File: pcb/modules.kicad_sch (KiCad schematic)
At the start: 20 parts, among them J2 Conn_01x08_Pin, J3 Conn_Coaxial, J4 Conn_Coaxial, Q2 2N7002, U4 BME280, U6 NEO-M8M, U7 E220-900T22S

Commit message: Finishing schematic and updating PCB
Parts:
- D2: footprint (none) -> LED_SMD:LED_Cree-XP-G
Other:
- moved on the sheet: C18, C19

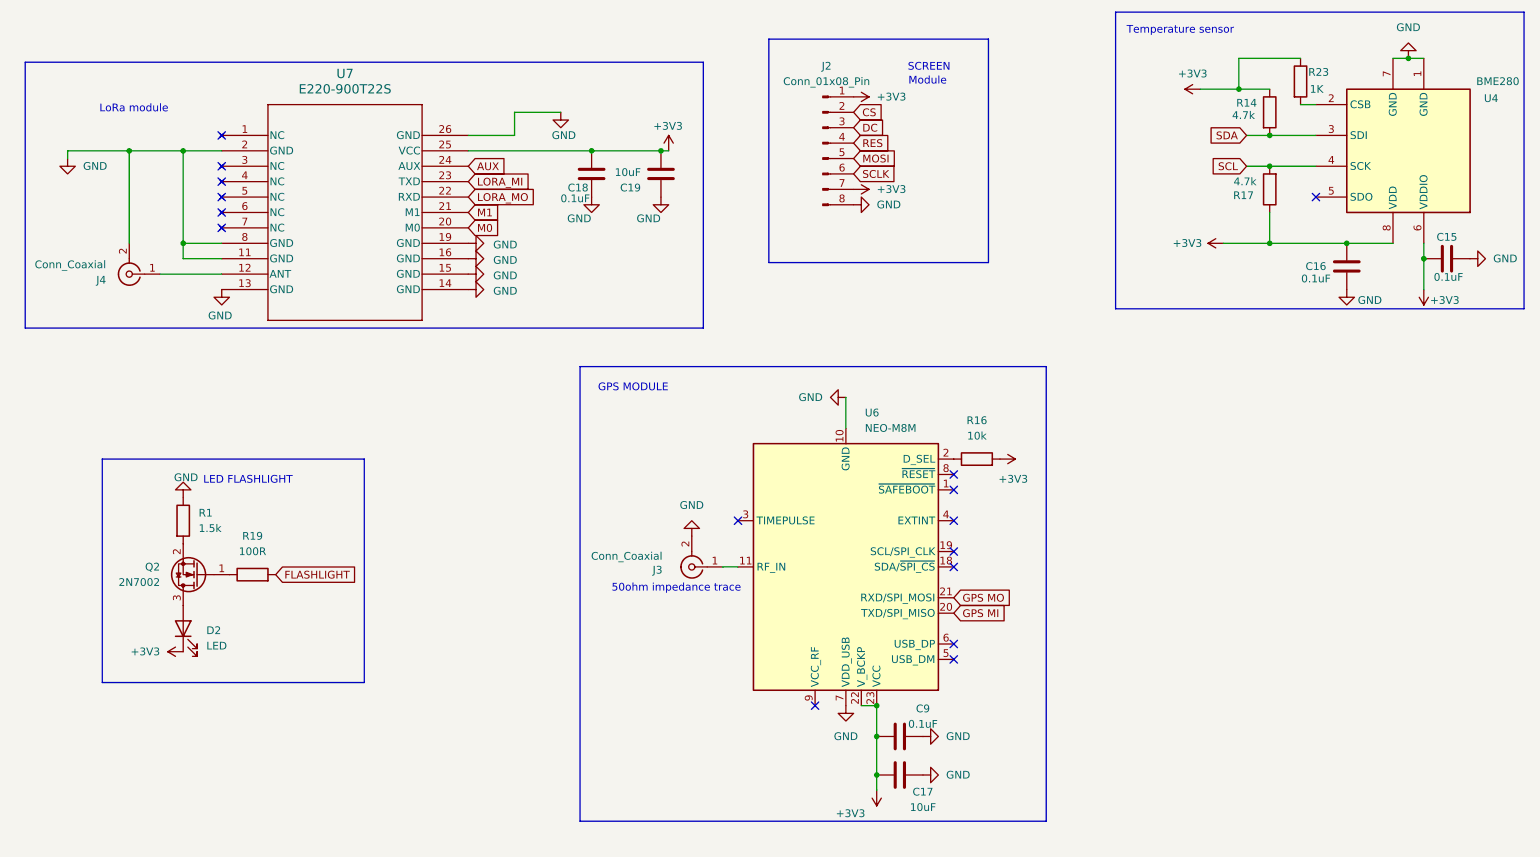
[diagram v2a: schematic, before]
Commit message: Fixing reversed polarity battery connector
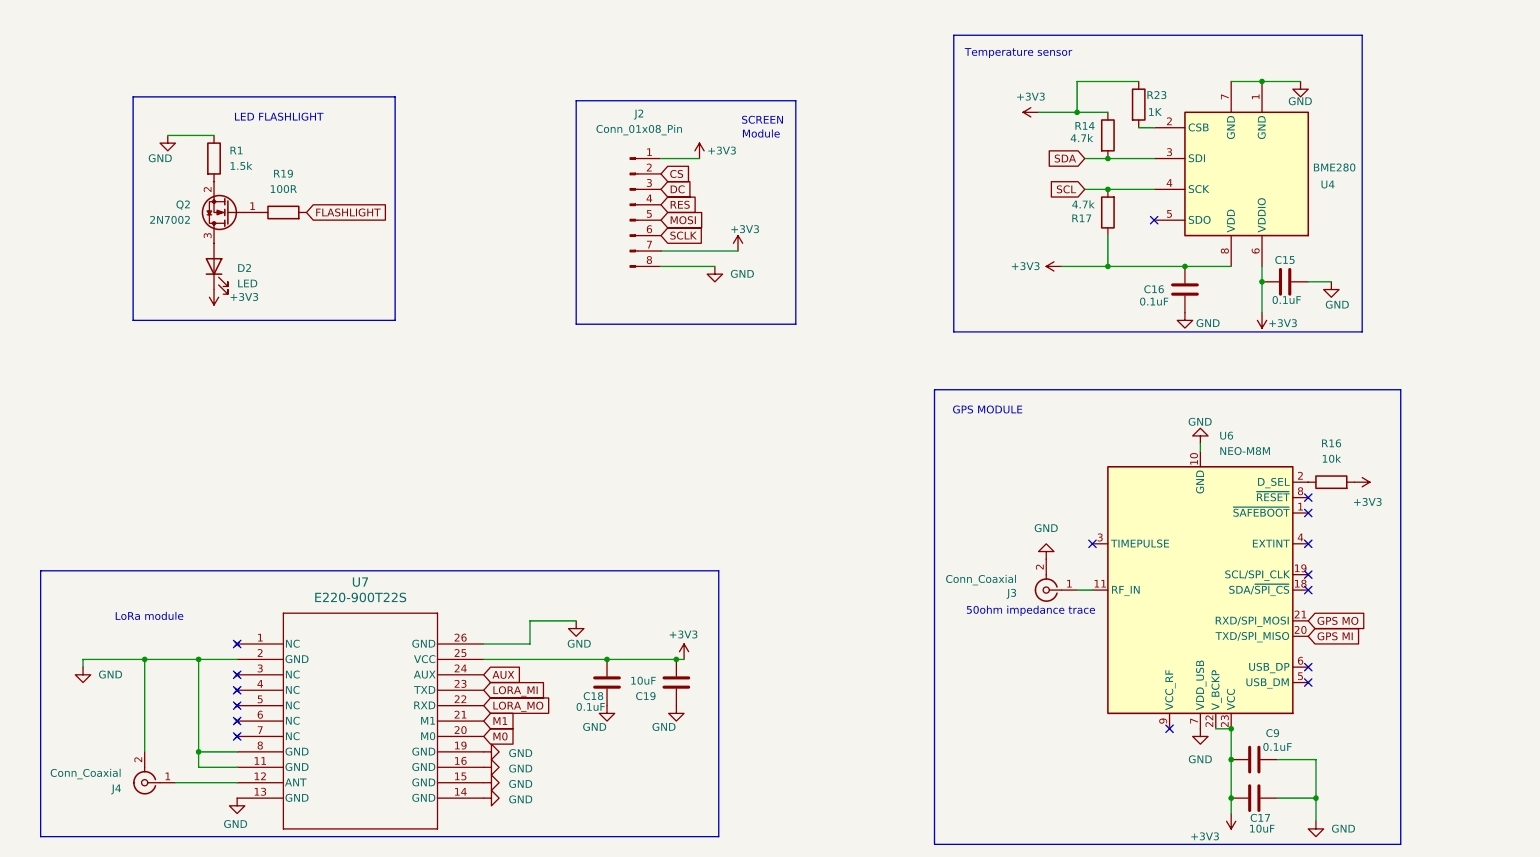
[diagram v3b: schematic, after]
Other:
- moved on the sheet: C15, C16, C17, C18, C19, C9, D2, J2, J3, J4, Q2, R1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

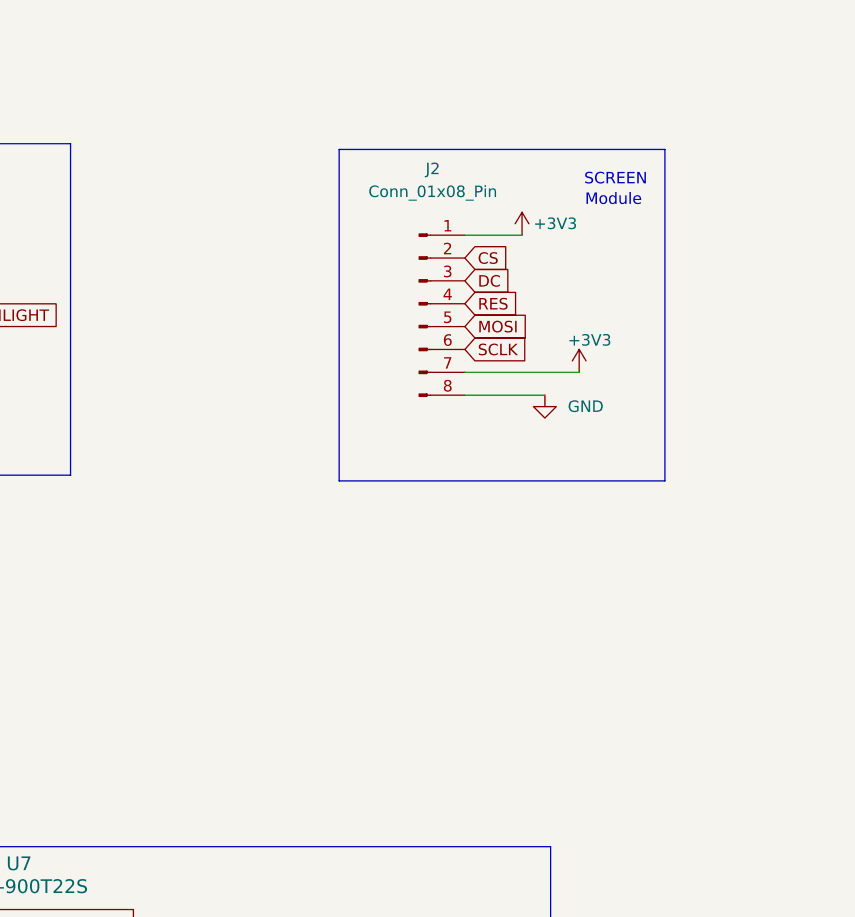
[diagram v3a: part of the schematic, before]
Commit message: Replacing screen pins by screen FPC connector
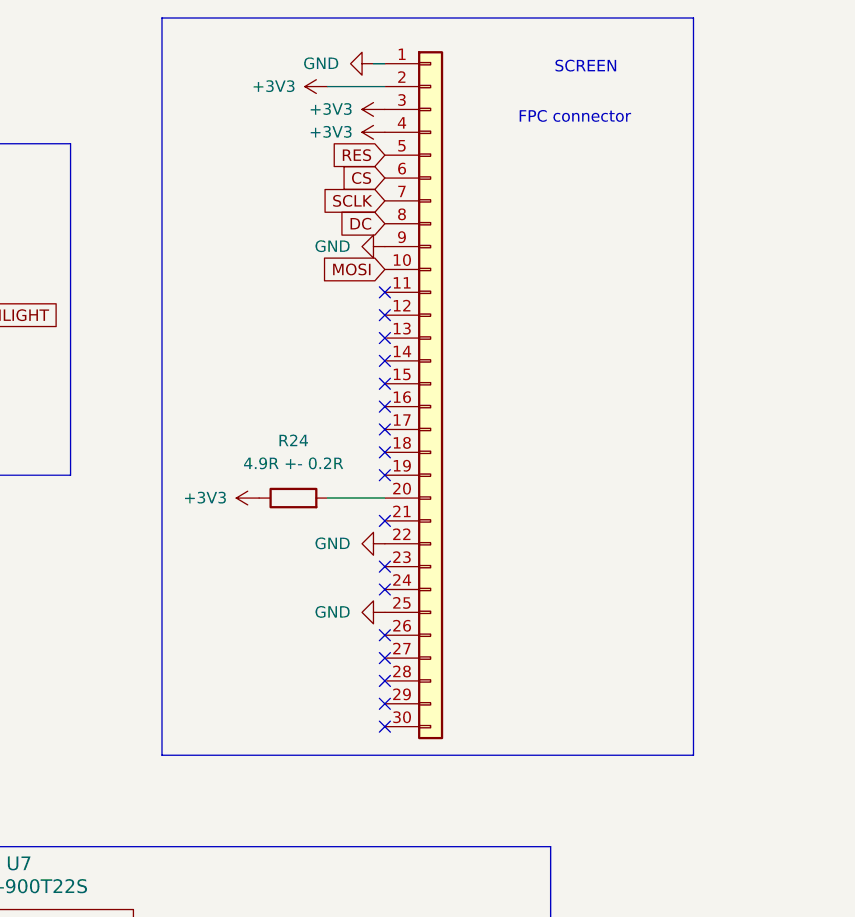
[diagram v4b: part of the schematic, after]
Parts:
- removed J2: Conn_01x08_Pin, Connector_PinHeader_1.00mm:PinHeader_1x08_P1.00mm_Vertical, symbol Connector:Conn_01x08_Pin
- added J6: Conn_01x30, Connector_FFC-FPC:Hirose_FH12-30S-0.5SH_1x30-1MP_P0.50mm_Horizontal, symbol Connector_Generic:Conn_01x30
- added R24: 4.9R +- 0.2R, Resistor_SMD:R_0805_2012Metric, symbol Device:R
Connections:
- net +3V3: now also J6.2 (Pin_2), J6.3 (Pin_3), J6.4 (Pin_4), R24.1
- net CS: now also J6.6 (Pin_6)
- net DC: now also J6.8 (Pin_8)
- net GND: now also J6.1 (Pin_1), J6.22 (Pin_22), J6.25 (Pin_25), J6.9 (Pin_9)
- net MOSI: now also J6.10 (Pin_10)
- net RES: now also J6.5 (Pin_5)
- net SCLK: now also J6.7 (Pin_7)
- new net: J6.20 (Pin_20), R24.2
- no-connect marks 16 -> 33
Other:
- note added: "FPC connector"
- note removed: "Module"
